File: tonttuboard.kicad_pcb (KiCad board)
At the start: 2 copper layers, 72.5 x 22.5 mm, 45 parts, among them U3 ICM-40609-D, U4 BMP388, U5 W25Q256JVFIQT, U6 MMC5983MA, U9 Teensy 4.0

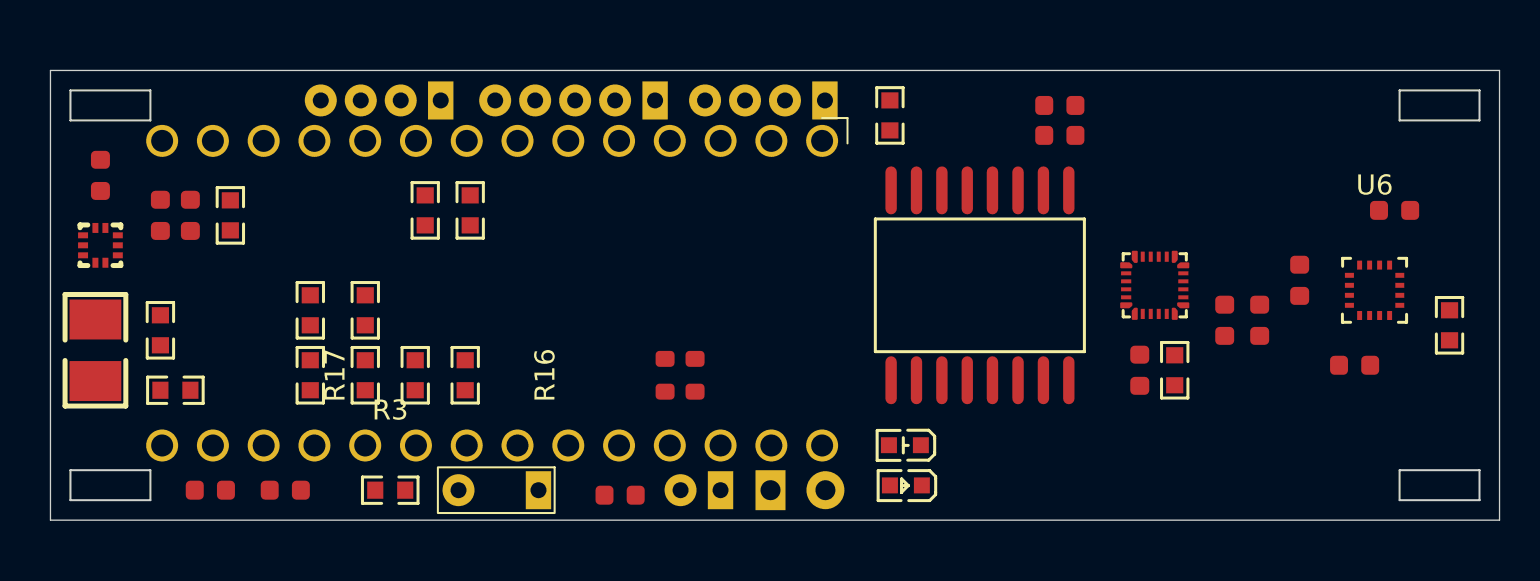
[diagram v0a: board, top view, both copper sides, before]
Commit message: Improved component placement
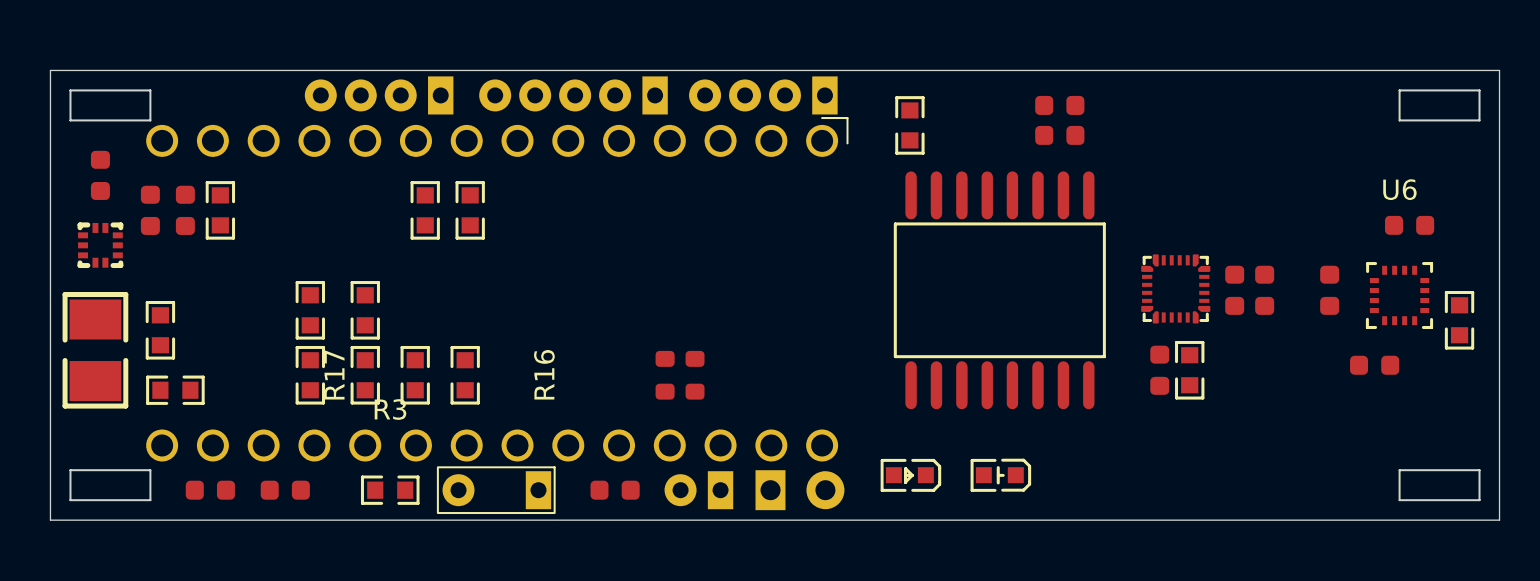
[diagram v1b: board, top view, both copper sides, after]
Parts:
- moved LED2 4.98 mm to (122.5, 95.2)
- moved C16 1.58 mm to (134.2, 86.0), turned to 90 degrees
- moved C8 1.58 mm to (139.0, 86.0)
- moved C2 1.52 mm to (135.8, 86.0), turned to 90 degrees
- moved U6 1.28 mm to (142.5, 86.3)
- moved R5 1.12 mm to (118.0, 77.8)
- moved U3 1.07 mm to (131.3, 85.9)
- moved C5 1.06 mm to (143.0, 82.8)
- moved U5 1.03 mm to (122.5, 86.0)
- moved C11 1.00 mm to (141.2, 89.8)
- moved C15 1.00 mm to (130.5, 90.0)
- moved R1 0.75 mm to (132.0, 90.0)
- moved C3 0.56 mm to (80.0, 82.0)
- moved R13 0.56 mm to (83.5, 82.0)
- moved R6 0.56 mm to (145.5, 87.5)
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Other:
- copper layers 2 -> 4

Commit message: Routed signals
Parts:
- moved R15 4.69 mm to (110.4, 90.0), turned to 0 degrees
- moved R19 3.48 mm to (110.5, 91.5), turned to 0 degrees
- moved R20 2.57 mm to (86.8, 89.2), turned to 0 degrees
- moved R21 2.30 mm to (90.2, 89.2), turned to 0 degrees
- moved R6 1.80 mm to (144.5, 86.0), turned to 90 degrees
- moved R12 1.60 mm to (86.8, 91.2), turned to 180 degrees
- moved C8 1.52 mm to (138.8, 84.5), turned to -90 degrees
- moved R13 1.52 mm to (85.0, 82.2), turned to 180 degrees
- moved U2 1.27 mm to (112.3, 96.2)
- moved U7 1.27 mm to (104.8, 96.2)
- moved R11 1.12 mm to (90.2, 91.2), turned to 0 degrees
- moved U10 1.06 mm to (119.8, 76.0)
- moved U6 1.00 mm to (141.5, 86.2)
- moved C14 0.90 mm to (102.5, 95.5)
- moved R5 0.90 mm to (117.5, 78.5), turned to 180 degrees
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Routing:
- net MISO: track 0.00 -> 131.4 mm, vias 0 -> 3
- net CLOCK: track 0.00 -> 74.0 mm, vias 0 -> 4
- net MOSI: track 0.00 -> 70.9 mm, vias 0 -> 4
- net CS_MAG: track 0.00 -> 62.8 mm, vias 0 -> 2
- net IMU_INT1: track 0.00 -> 52.5 mm, vias 0 -> 2
- net IMU_INT2: track 0.00 -> 47.8 mm
- net MAG_INT: track 0.00 -> 44.7 mm, vias 0 -> 2
- net CS_IMU: track 0.00 -> 39.5 mm, vias 0 -> 2
- net CS_FLASH: track 0.00 -> 36.3 mm, vias 0 -> 2
- net SCL: track 0.00 -> 30.9 mm
- net BARO_INT: track 0.00 -> 26.3 mm
- net SDA: track 0.00 -> 26.2 mm, vias 0 -> 2
- net +3.3V: track 0.00 -> 21.5 mm
- net LDR_READ: track 0.00 -> 16.4 mm
- net GND: track 0.00 -> 15.3 mm
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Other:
- board size 72.5 x 22.5 mm -> 71.5 x 23.5 mm

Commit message: Added gnd vias and decorated
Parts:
- added G***: LOGO, Graphics:mag_orientation_6x5,5, F.Cu at (140.5, 79.2)
- added G***: LOGO, Graphics:imu_orientation_6,5x5, F.Cu at (140.8, 92.2)
- added G***: LOGO, Graphics:ekotomtarna_nino_logo_22x22_positive, B.Cu at (127.2, 85.4)
- moved C5 8.00 mm to (136.2, 78.0)
- moved U6 7.52 mm to (136.0, 81.1)
- moved C15 7.52 mm to (137.8, 88.0), turned to 180 degrees
- moved C8 7.48 mm to (133.0, 79.7)
- moved C11 7.46 mm to (135.8, 84.0)
- moved C2 7.08 mm to (131.0, 91.2), turned to -90 degrees
- moved U3 6.94 mm to (135.8, 91.2), turned to 180 degrees
- moved R6 6.37 mm to (138.8, 83.2), turned to -90 degrees
- moved C16 5.53 mm to (132.5, 91.2), turned to -90 degrees
- moved R5 5.39 mm to (115.5, 83.5)
- moved C4 5.30 mm to (78.2, 85.5), turned to 0 degrees
- moved C1 4.78 mm to (77.0, 82.8)
- moved C3 4.53 mm to (75.5, 82.8)
- moved R1 4.10 mm to (135.2, 87.5), turned to 90 degrees
- moved U4 2.02 mm to (79.2, 82.8), turned to 180 degrees
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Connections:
- R10 pad 1: CS_IMU -> CS_MAG
- R12 pad 2: CS_MAG -> CS_IMU
- R20 pad 1: CS_MAG -> CS_IMU
- R9 pad 1: CS_IMU -> CS_MAG
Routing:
- net MISO: track 131.4 -> 65.0 mm, vias 3 -> 2
- net GND: track 15.3 -> 50.0 mm, vias 0 -> 54
- net +3.3V: track 21.5 -> 48.6 mm, vias 0 -> 20
- net IMU_INT2: track 47.8 -> 66.6 mm, vias 0 -> 2
- net CS_IMU: track 39.5 -> 56.0 mm
- net CS_MAG: track 62.8 -> 54.5 mm
- net IMU_INT1: track 52.5 -> 59.9 mm
- net SCL: track 30.9 -> 23.6 mm, vias 0 -> 2
- net SDA: track 26.2 -> 21.1 mm
- net MOSI: track 70.9 -> 75.9 mm, vias 4 -> 2
- net MAG_INT: track 44.7 -> 39.7 mm
- net CLOCK: track 74.0 -> 78.2 mm, vias 4 -> 0
- net CS_FLASH: track 36.3 -> 38.7 mm
- net BARO_INT: track 26.3 -> 28.4 mm, vias 0 -> 2
- net Net-(LED1-A): track 7.68 -> 6.02 mm
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- added copper zone on In2.Cu, net +3.3V
- added copper zone on In1.Cu, net GND
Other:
- board size 71.5 x 23.5 mm -> 70 x 25 mm
- board text added: "3V"
- board text added: "5V"
- board text added: "BARO"
- board text added: "BAT_READ"
- board text added: "EKOTOMTARNA"
- board text added: "FLASH MEMORY"
- board text added: "IMU"
- board text added: "M1"
- board text added: "M2"
- board text added: "M3"
- board text added: "M4"
- board text added: "MAGNETO- METER"
- board text added: "NO EMI PLS"
- board text added: "PWR"
- board text added: "RX"
- board text added: "STATE"
- board text added: "THERM."
- board text added: "TONTTUBOARD"
- board text added: "TX"
- board text added: "USB"
- board text added: "{dblquote}DESIGNED{dblquote} BY OSKAR HUOTARI"

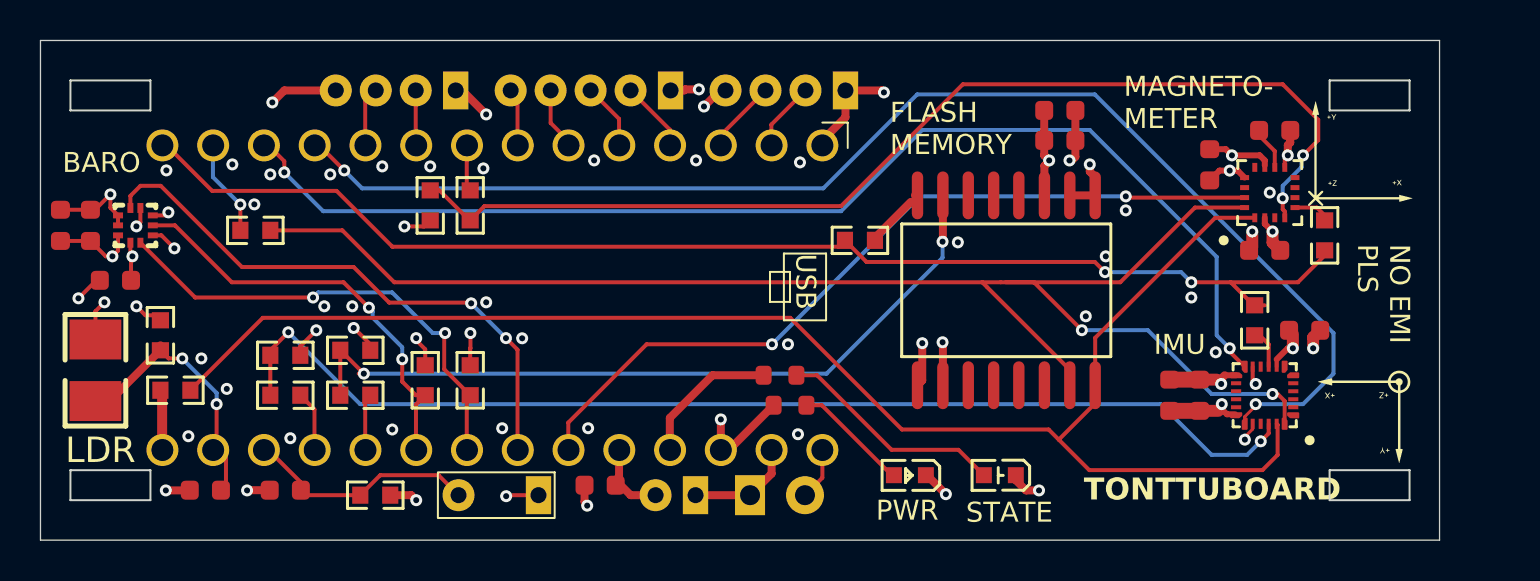
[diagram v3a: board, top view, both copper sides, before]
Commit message: Improved clearances and silkscreen, added copper fill on l4 and vias
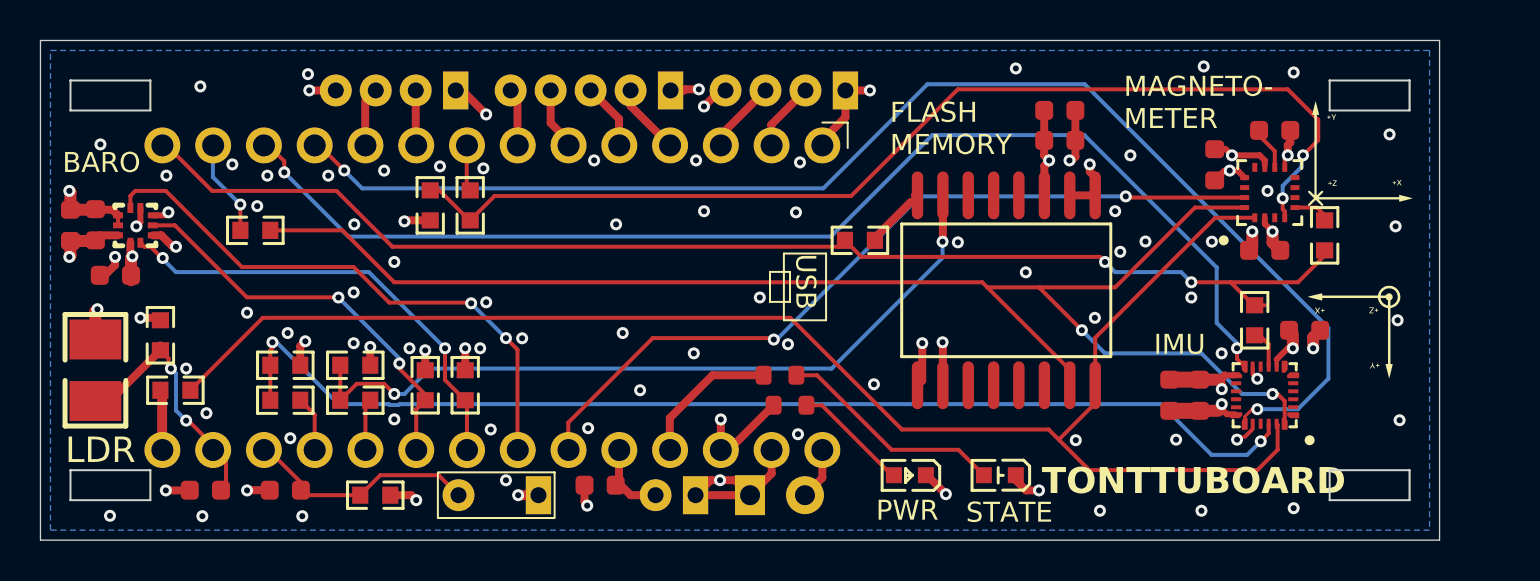
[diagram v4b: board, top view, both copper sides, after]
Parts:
- moved G*** 4.28 mm to (140.2, 88.0)
- moved R21 0.75 mm to (90.2, 89.8)
- moved C3 0.50 mm to (76.0, 82.8)
- moved R20 0.50 mm to (86.8, 89.8)
- moved R16 0.35 mm to (95.8, 90.8)
- moved C1 0.25 mm to (77.2, 82.7)
- moved C4 0.25 mm to (78.2, 85.2)
- moved C8 0.25 mm to (133.2, 79.7)
- moved R11 0.25 mm to (90.2, 91.5)
- moved R12 0.25 mm to (86.8, 91.5)
- moved R17 0.25 mm to (93.8, 90.8)
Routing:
- net +3.3V: track 48.6 -> 43.0 mm
- net MOSI: track 75.9 -> 74.0 mm
- net GND: track 50.0 -> 51.9 mm, vias 54 -> 91
- net IMU_INT1: track 59.9 -> 60.5 mm
- net SDA: track 21.1 -> 20.5 mm
- added copper zone on B.Cu, net GND
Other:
- board text removed: "NO EMI PLS"

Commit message: Replaced LDR with a through hole due to a soldering temperature issue. Also made the thermistor silk screen better and fixed a typo. Added CanSat 2026 Vaasa text to the back silkscreen
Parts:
- removed R18: GT36516, EasyEDA:RES-SMD_L3.6-W2.4
- added R2: R_Photo, Ossi connectors:LDR-holes, F.Cu at (77.5, 83.5)
- R4: value 0603WAF1002T5E -> 22kΩ; footprint EasyEDA:R0603 -> PCM_JLCPCB:R_0603
- TH1: footprint Ossi connectors:Thermisto-place -> Ossi connectors:Thermistor-holes
- moved C3 0.25 mm to (75.8, 82.8)
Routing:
- net GND: track 51.9 -> 51.1 mm
- net +3.3V: track 43.0 -> 42.5 mm, vias 20 -> 19
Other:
- board text added: "CANSAT 2026 VAASA"
- board text removed: "EKOTOMTARNA"

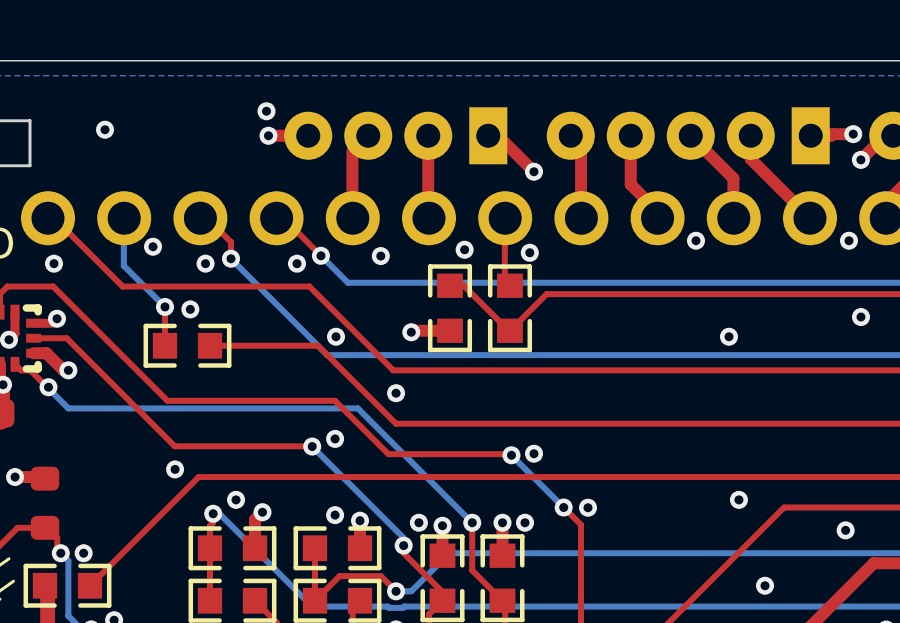
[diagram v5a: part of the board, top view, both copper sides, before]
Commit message: Changed the CS Magnetometer 100 kohm pull-up to 4.7 kohm pulldown
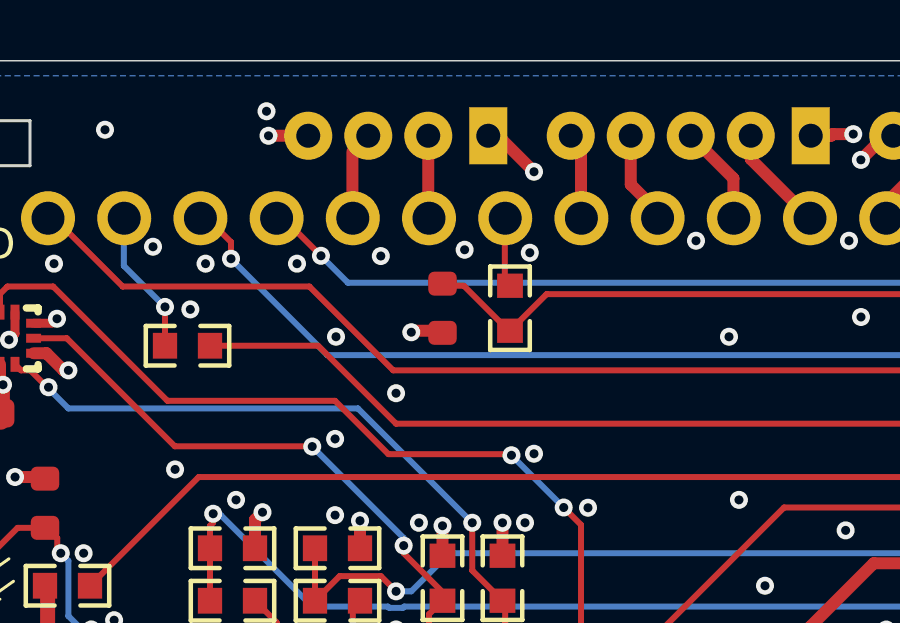
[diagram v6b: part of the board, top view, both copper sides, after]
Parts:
- removed R9: 0603WAF1003T5E, EasyEDA:R0603
- added R7: 4.7kΩ, PCM_JLCPCB:R_0603, F.Cu at (93.8, 81.8)
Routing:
- net +3.3V: track 42.5 -> 41.1 mm, vias 19 -> 18
- net GND: track 51.1 -> 52.4 mm, vias 91 -> 92

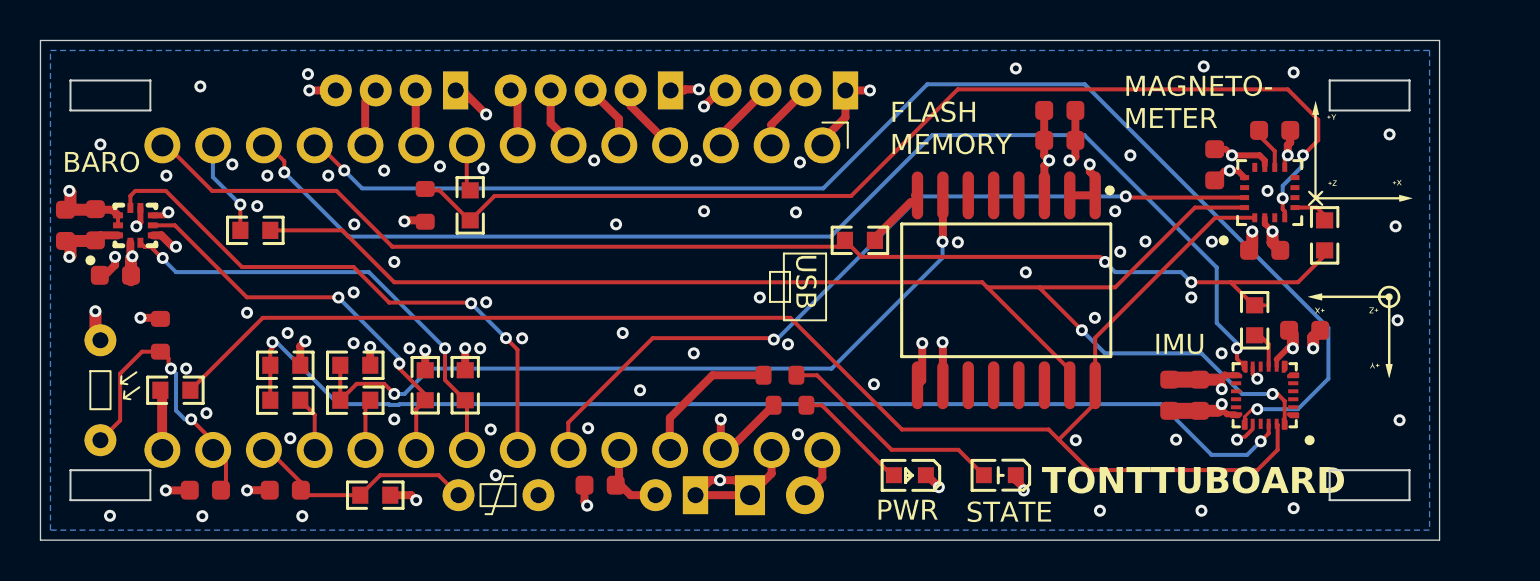
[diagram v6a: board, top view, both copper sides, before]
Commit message: Removed magnetometer and changed component placement
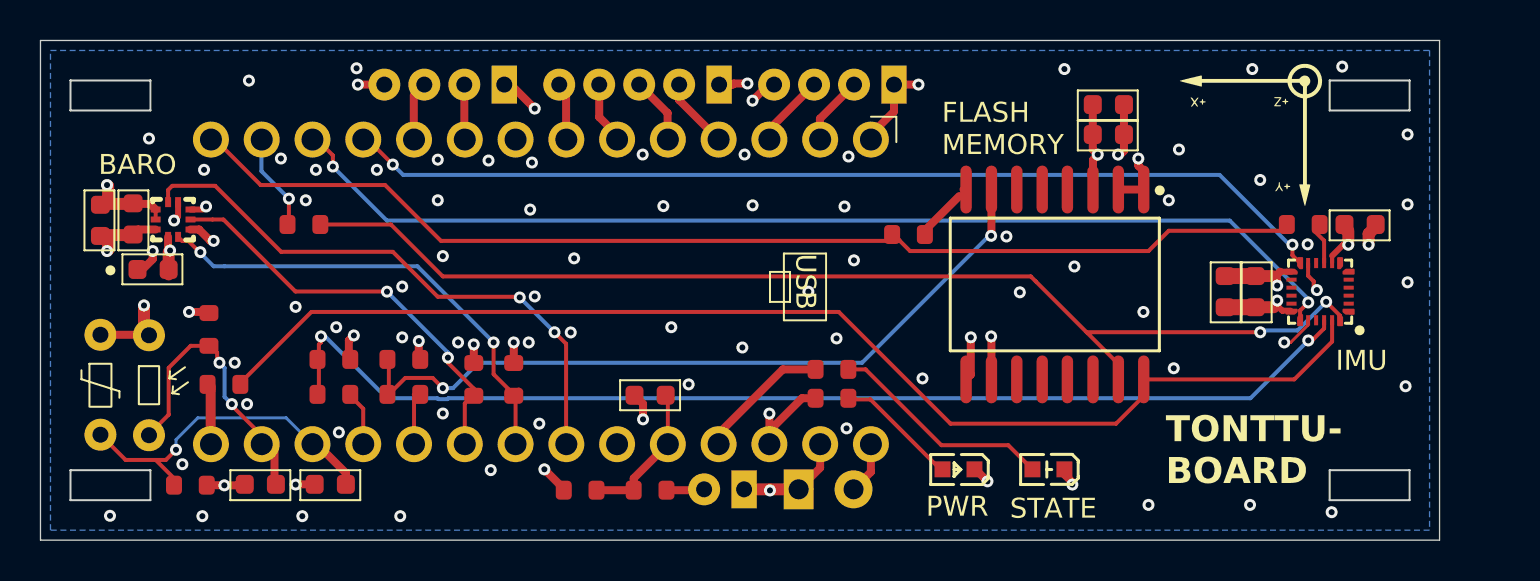
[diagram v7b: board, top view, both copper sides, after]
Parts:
- removed C11: 1uF, PCM_JLCPCB:C_0603
- removed C5: 10uF, PCM_JLCPCB:C_0603
- removed C8: 100nF, PCM_JLCPCB:C_0603
- removed the G*** at (140.5, 79.2)
- removed the G*** at (140.2, 88.0)
- removed R10: RC0603FR-0733RL, EasyEDA:R0603
- removed U6: MMC5983MA, EasyEDA:LGA-16_L3.0-W3.0-P0.50-BL_SQ
- added G***: LOGO, Graphics:imu_orientation_10x7,7, F.Cu at (135.1, 78.1)
- R1, R11, R12, R13, R14, R5: value RC0603FR-0733RL -> 33Ω; footprint EasyEDA:R0603 -> PCM_JLCPCB:R_0603
- R16, R17: value 0603WAF2701T5E -> 2.7kΩ; footprint EasyEDA:R0603 -> PCM_JLCPCB:R_0603
- R20, R21: value 0603WAF1003T5E -> 100kΩ; footprint EasyEDA:R0603 -> PCM_JLCPCB:R_0603
- R3: footprint EasyEDA:R0603 -> PCM_JLCPCB:R_0603
- R6: value RC0603FR-0733RL -> 18kΩ; footprint EasyEDA:R0603 -> PCM_JLCPCB:R_0603
- R7: value 4.7kΩ -> 10kΩ
- moved R6 36.1 mm to (105.0, 96.0), turned to 0 degrees
- moved TH1 29.9 mm to (77.5, 83.2), turned to 0 degrees
- moved R7 16.2 mm to (101.5, 96.0), turned to 0 degrees
- moved R3 9.26 mm to (82.0, 95.8)
- moved C15 5.98 mm to (140.5, 82.7)
- moved C16 5.88 mm to (135.3, 86.1)
- moved C2 5.88 mm to (133.8, 86.1)
- moved U3 5.88 mm to (138.5, 86.1)
- moved R1 5.37 mm to (137.7, 82.7), turned to 180 degrees
- moved C14 5.15 mm to (105.0, 91.2)
- moved C13 2.77 mm to (85.5, 95.7)
- moved R15 2.62 mm to (114.1, 90.0)
- moved C10 2.45 mm to (127.9, 76.7)
- moved C9 2.45 mm to (127.9, 78.2)
- moved LED1 2.45 mm to (120.4, 95.0)
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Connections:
- R6 pad 1: Net-(U6-SPI_SDO) -> BAT_READ
- R6 pad 2: MISO -> Net-(U2-BAT_POS)
- R7 pad 2: CS_MAG -> BAT_READ
- U2 pad 2: BAT_READ -> Net-(U2-BAT_POS)
- U9 pad 11: IMU_INT2 -> IMU_INT1
- U9 pad 12: IMU_INT1 -> IMU_INT2
- U9 pad 28: MAG_INT -> unconnected-(U9-21_A7_RX5_BCLK1-Pad28)
- U9 pad 8: Net-(U9-6_OUT1D) -> unconnected-(U9-6_OUT1D-Pad8)
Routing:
- net CS_MAG: track 54.3 -> 0.00 mm, vias 2 -> 0
- net MAG_INT: track 39.7 -> 0.00 mm, vias 2 -> 0
- net MOSI: track 74.0 -> 57.5 mm
- net CLOCK: track 78.1 -> 63.6 mm
- net IMU_INT2: track 66.8 -> 54.8 mm
- net IMU_INT1: track 60.5 -> 50.0 mm
- net GND: track 52.4 -> 44.0 mm, vias 92 -> 88
- net MISO: track 65.0 -> 57.6 mm, vias 2 -> 0
- net TEMP_READ: track 11.8 -> 17.7 mm, vias 0 -> 1
- net BAT_READ: track 4.13 -> 7.36 mm
- net Net-(U9-6_OUT1D): track 2.56 -> 0.00 mm
- net Net-(U6-CAP): track 1.93 -> 0.00 mm
- net Net-(U2-BAT_POS): track 0.00 -> 1.90 mm
- net +3.3V: track 41.1 -> 39.3 mm, vias 18 -> 16
- net Net-(U6-SPI_SDO): track 1.65 -> 0.00 mm
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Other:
- board text added: "CANSAT 2026 FINLAND"
- board text added: "TONTTU- BOARD"
- board text removed: "CANSAT 2026 VAASA"
- board text removed: "MAGNETO- METER"
- board text removed: "THERM."
- board text removed: "TONTTUBOARD"
